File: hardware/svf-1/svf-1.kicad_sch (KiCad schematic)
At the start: 75 parts, among them J1 MonoJack, J2 MonoJack, J3 MonoJack, J4 MonoJack, J5 MonoJack, J6 MonoJack, J7 MonoJack, J8 MonoJack, J9 IDC Header 10P, Q1 MMDT5401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

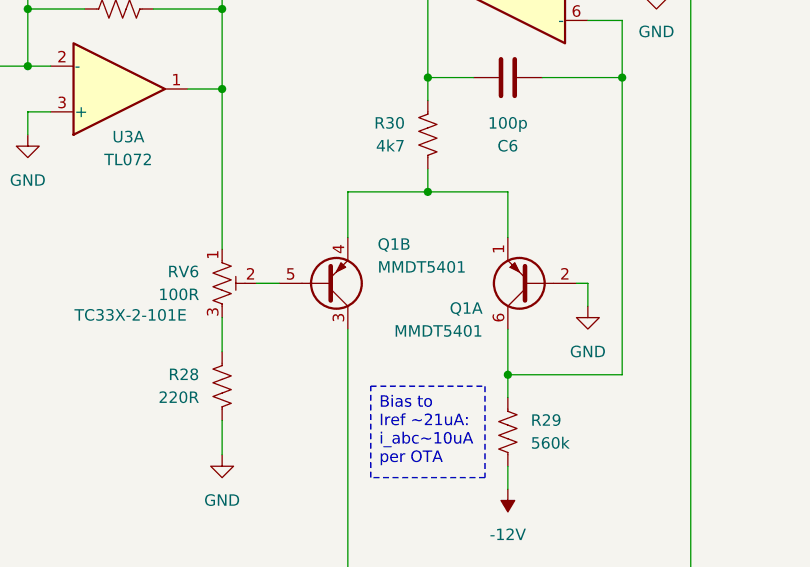
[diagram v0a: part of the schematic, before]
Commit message: Schematic and PBC fix: replace incorrect MMDT5401 (SOT-363) with DMMT5401 (SOT-236) part
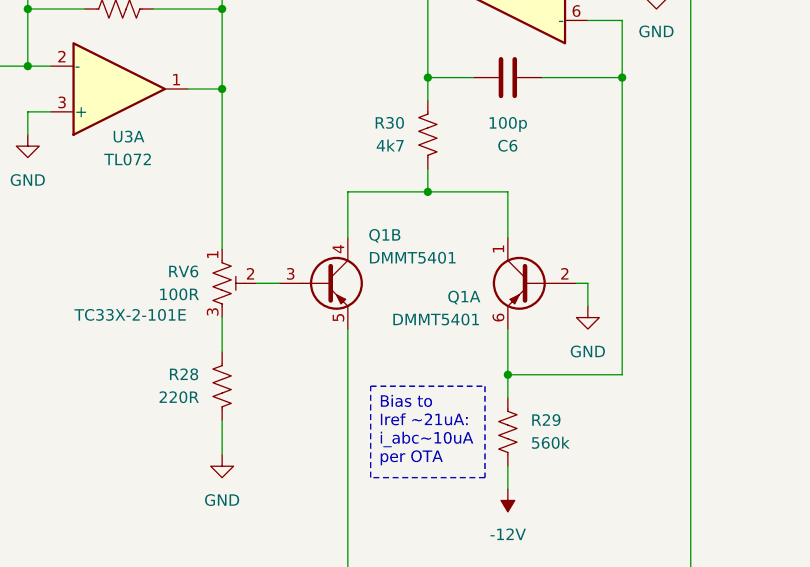
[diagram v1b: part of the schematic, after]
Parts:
- removed Q1: MMDT5401, Package_TO_SOT_SMD:SOT-363_SC-70-6, symbol Transistor_BJT:MMDT5401
- added Q1: DMMT5401, Package_TO_SOT_SMD:SOT-23-6, symbol Transistor_BJT:DMMT5401
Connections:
- net GND: now also Q1.2 (B1)
- net at C6.1, R29.2, U3.6 (-): now also Q1.6 (E1)
- net at R30.1: now also Q1.1 (C1), Q1.4 (C2)
- net at R17.1, R9.1: now also Q1.5 (E2)
- net at RV6.2: now also Q1.3 (B2)
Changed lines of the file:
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@@
 	(title_block
 		(title "State Variable Filter")
-		(date "2025-12-14")
-		(rev "1.0")
+		(date "2025-12-28")
+		(rev "1.1")
 		(company "idyllm")
 		(comment 1 "CC BY-SA 4.0")
@@
 	)
 	(symbol
+		(lib_id "Transistor_BJT:DMMT5401")
+		(at 120.65 168.91 0)
+		(mirror y)
+		(unit 1)
+		(exclude_from_sim no)
+		(in_bom yes)
+		(on_board yes)
+		(dnp no)
+		(property "Reference" "Q1"
+			(at 115.062 170.434 0)
+			(effects
+				(font
+					(size 1.27 1.27)
+				)
+				(justify left)
+			)
+		)
+		(property "Value" "DMMT5401"
+			(at 115.062 172.974 0)
+			(effects
+				(font
+					(size 1.27 1.27)
+				)
+				(justify left)
+			)
+		)
+		(property "Footprint" "Package_TO_SOT_SMD:SOT-23-6"
+			(at 115.57 166.37 0)
+			(effects
+				(font
+					(size 1.27 1.27)
+				)
+				(hide yes)
+			)
+		)
+		(property "Datasheet" "https://www.diodes.com/assets/Datasheets/ds30437.pdf"
+			(at 120.65 168.91 0)
+			(effects
+				(font
+					(size 1.27 1.27)
+				)
+				(hide yes)
+			)
+		)
+		(property "Description" "Dual PNP transistor, 6 pin package"
+			(at 120.65 168.91 0)
+			(effects
+				(font
+					(size 1.27 1.27)
+				)
+				(hide yes)
+			)
+		)
+		(pin "1"
+		)
+		(pin "4"
+		)
+		(pin "3"
+		)
+		(pin "6"
+		)
+		(pin "5"
+		)
+		(pin "2"
+		)
+		(instances
+			(project ""
+				(path "/eb791da7-766f-42cc-8763-47037328a8d4"
+					(reference "Q1")
+					(unit 1)
+				)
+			)
+		)
+	)
+	(symbol
 		(lib_id "Device:C")
 		(at 217.17 156.21 0)
@@
 	)
 	(symbol
+		(lib_id "Transistor_BJT:DMMT5401")
+		(at 97.79 168.91 0)
+		(unit 2)
+		(exclude_from_sim no)
+		(in_bom yes)
+		(on_board yes)
+		(dnp no)
+		(property "Reference" "Q1"
+			(at 102.616 163.576 0)
+			(effects
+				(font
+					(size 1.27 1.27)
+				)
+				(justify left)
+			)
+		)
+		(property "Value" "DMMT5401"
+			(at 102.616 166.116 0)
+			(effects
+				(font
+					(size 1.27 1.27)
+				)
+				(justify left)
+			)
+		)
+		(property "Footprint" "Package_TO_SOT_SMD:SOT-23-6"
+			(at 102.87 166.37 0)
+			(effects
+				(font
+					(size 1.27 1.27)
+				)
+				(hide yes)
+			)
+		)
+		(property "Datasheet" "https://www.diodes.com/assets/Datasheets/ds30437.pdf"
+			(at 97.79 168.91 0)
+			(effects
+				(font
+					(size 1.27 1.27)
+				)
+				(hide yes)
+			)
+		)
+		(property "Description" "Dual PNP transistor, 6 pin package"
+			(at 97.79 168.91 0)
+			(effects
+				(font
+					(size 1.27 1.27)
+				)
+				(hide yes)
+			)
+		)
+		(pin "1"
+		)
+		(pin "4"
+		)
+		(pin "3"
+		)
+		(pin "6"
+		)
+		(pin "5"
+		)
+		(pin "2"
+		)
+		(instances
+			(project ""
+				(path "/eb791da7-766f-42cc-8763-47037328a8d4"
+					(reference "Q1")
+					(unit 2)
+				)
+			)
+		)
+	)
+	(symbol
 		(lib_id "Device:C")
 		(at 118.11 146.05 270)
@@
 	)
 	(symbol
-		(lib_id "Transistor_BJT:MMDT5401")
-		(at 120.65 168.91 180)
-		(unit 1)
-		(exclude_from_sim no)
-		(in_bom yes)
-		(on_board yes)
-		(dnp no)
-		(property "Reference" "Q1"
-			(at 115.316 171.704 0)
-			(effects
-				(font
-					(size 1.27 1.27)
-				)
-				(justify left)
-			)
-		)
-		(property "Value" "MMDT5401"
-			(at 115.316 174.244 0)
-			(effects
-				(font
-					(size 1.27 1.27)
-				)
-				(justify left)
-			)
-		)
-		(property "Footprint" "Package_TO_SOT_SMD:SOT-363_SC-70-6"
-			(at 115.57 171.45 0)
-			(effects
-				(font
-					(size 1.27 1.27)
-				)
-				(hide yes)
-			)
-		)
-		(property "Datasheet" "http://www.diodes.com/_files/datasheets/ds30169.pdf"
-			(at 120.65 168.91 0)
-			(effects
-				(font
-					(size 1.27 1.27)
-				)
-				(hide yes)
-			)
-		)
-		(property "Description" "200mA IC, 160V Vce, Dual PNP/PNP Transistors, SOT-363"
-			(at 120.65 168.91 0)
-			(effects
-				(font
-					(size 1.27 1.27)
-				)
-				(hide yes)
-			)
-		)
-		(pin "1"
-		)
-		(pin "6"
-		)
-		(pin "4"
-		)
-		(pin "5"
-		)
-		(pin "3"
-		)
-		(pin "2"
-		)
-		(instances
-			(project ""
-				(path "/eb791da7-766f-42cc-8763-47037328a8d4"
-					(reference "Q1")
-					(unit 1)
-				)
-			)
-		)
-	)
-	(symbol
 		(lib_id "Amplifier_Operational:TL074")
 		(at 152.4 77.47 0)
@@
 				)
 			)
-		)
-	)
-	(symbol
-		(lib_id "Transistor_BJT:MMDT5401")
-		(at 97.79 168.91 0)
-		(mirror x)
-		(unit 2)
-		(exclude_from_sim no)
-		(in_bom yes)
-		(on_board yes)
-		(dnp no)
-		(property "Reference" "Q1"
-			(at 103.632 164.592 0)
-			(effects
-				(font
-					(size 1.27 1.27)
-				)
-				(justify left)
-			)
-		)
-		(property "Value" "MMDT5401"
-			(at 103.632 167.132 0)
-			(effects
-				(font
-					(size 1.27 1.27)
-				)
-				(justify left)
-			)
-		)
-		(property "Footprint" "Package_TO_SOT_SMD:SOT-363_SC-70-6"
-			(at 102.87 171.45 0)
-			(effects
-				(font
-					(size 1.27 1.27)
-				)
-				(hide yes)
-			)
-		)
-		(property "Datasheet" "http://www.diodes.com/_files/datasheets/ds30169.pdf"
-			(at 97.79 168.91 0)
-			(effects
-				(font
-					(size 1.27 1.27)
-				)
-				(hide yes)
-			)
-		)
-		(property "Description" "200mA IC, 160V Vce, Dual PNP/PNP Transistors, SOT-363"
-			(at 97.79 168.91 0)
-			(effects
-				(font
-					(size 1.27 1.27)
-				)
-				(hide yes)
-			)
-		)
-		(pin "1"
-		)
-		(pin "6"
-		)
-		(pin "4"
-		)
-		(pin "5"
-		)
-		(pin "3"
-		)
-		(pin "2"
-		)
-		(instances
-			(project ""
-				(path "/eb791da7-766f-42cc-8763-47037328a8d4"
-					(reference "Q1")
-					(unit 2)
-				)
-			)

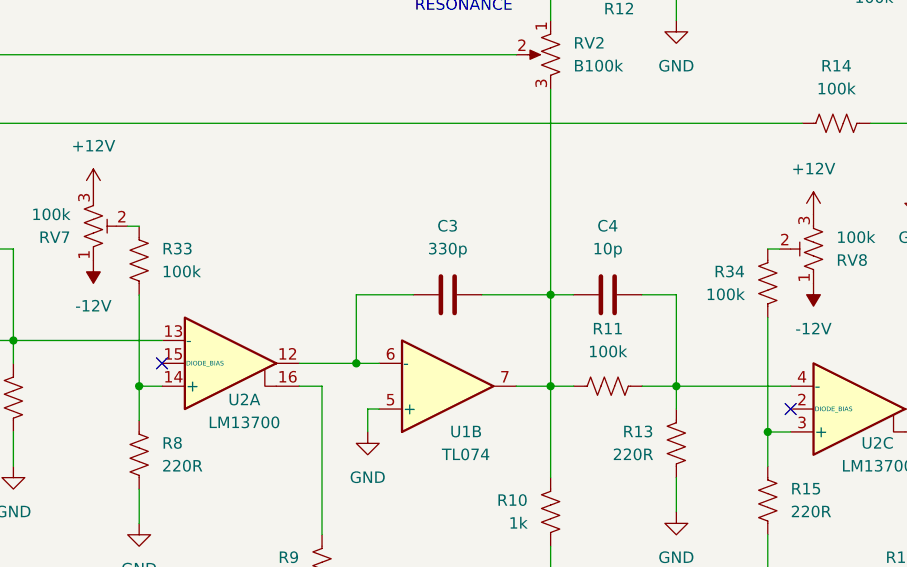
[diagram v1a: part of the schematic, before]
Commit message: Updated docs and design after building and testing the PCB
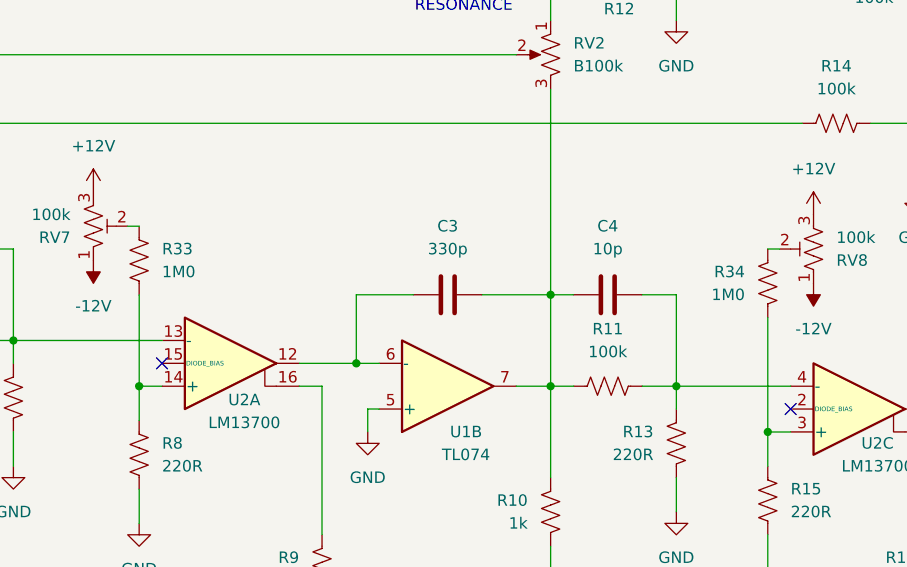
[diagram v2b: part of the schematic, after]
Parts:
- R33, R34: value 100k -> 1M0
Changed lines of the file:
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@@
 	(title_block
 		(title "State Variable Filter")
-		(date "2025-12-28")
+		(date "2026-01-02")
 		(rev "1.1")
 		(company "idyllm")
@@
 			)
 		)
-		(property "Value" "100k"
+		(property "Value" "1M0"
 			(at 185.42 67.3099 0)
 			(effects
@@
 			)
 		)
-		(property "Value" "100k"
+		(property "Value" "1M0"
 			(at 120.65 64.7699 0)
 			(effects

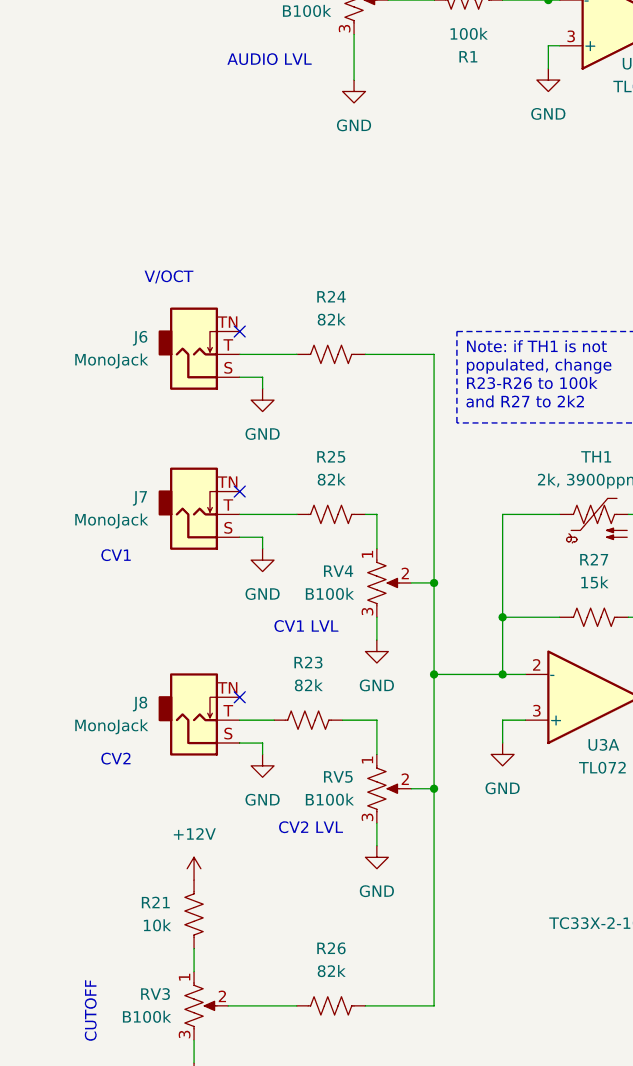
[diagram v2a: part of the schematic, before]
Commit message: Fix CV input pots and Rs
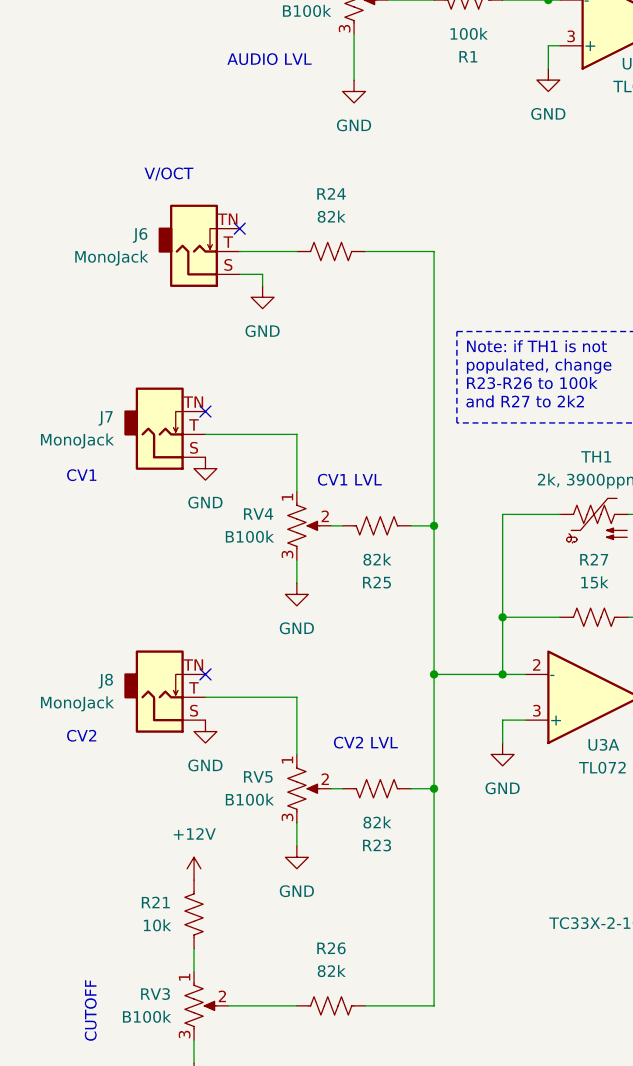
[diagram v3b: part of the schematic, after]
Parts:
- Q1: footprint Package_TO_SOT_SMD:SOT-23-6 -> Package_TO_SOT_SMD:SOT-23-6_Handsoldering
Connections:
- net at RV5.1: now also J8.T; no longer R23.2
- net at R24.2, R26.2, R27.1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: now also R23.2, R25.2; no longer RV4.2, RV5.2
- net at R23.1: now also RV5.2; no longer J8.T
- net at RV4.1: now also J7.T; no longer R25.2
- net at R25.1: now also RV4.2; no longer J7.T
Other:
- moved on the sheet: J6, J7, J8, R23, R24, R25, RV4, RV5

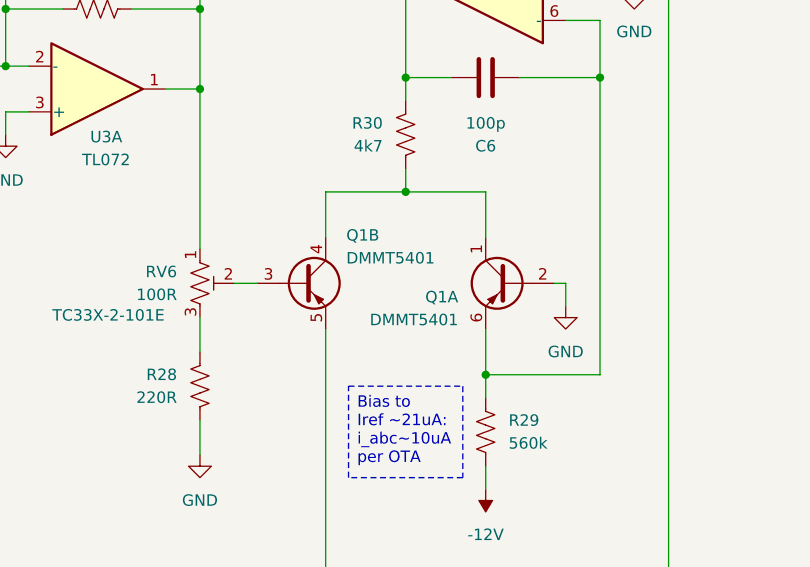
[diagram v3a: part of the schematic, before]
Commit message: Fix for flipped PNP wiring
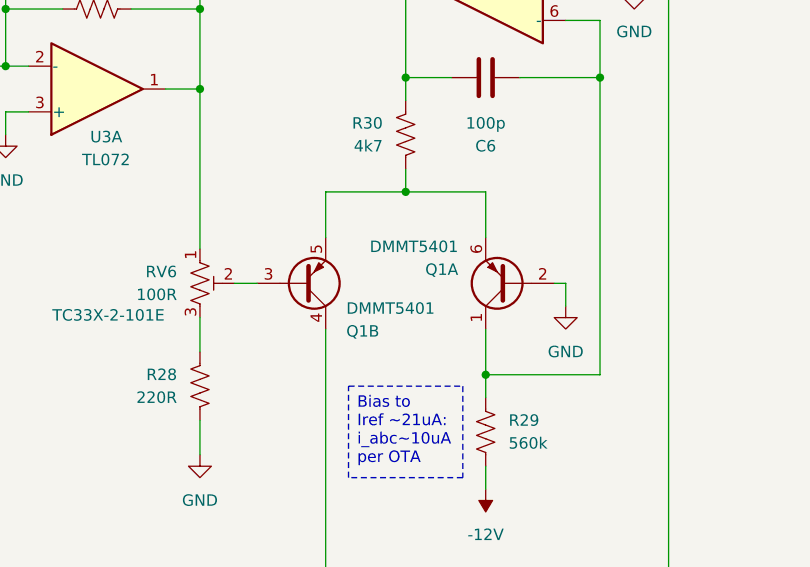
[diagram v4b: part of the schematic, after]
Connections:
- net at C6.1, R29.2, U3.6 (-): now also Q1.1 (C1); no longer Q1.6 (E1)
- net at R17.1, R9.1: now also Q1.4 (C2); no longer Q1.5 (E2)
- new net: Q1.5 (E2), Q1.6 (E1), R30.1
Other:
- moved on the sheet: Q1A
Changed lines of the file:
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@@
 	(title_block
 		(title "State Variable Filter")
-		(date "2026-01-03")
-		(rev "1.1")
+		(date "2026-02-10")
+		(rev "1.2")
 		(company "idyllm")
 		(comment 1 "CC BY-SA 4.0")
@@
 	(symbol
 		(lib_id "Transistor_BJT:DMMT5401")
-		(at 120.65 168.91 0)
-		(mirror y)
+		(at 120.65 168.91 180)
 		(unit 1)
 		(exclude_from_sim no)
@@
 		(dnp no)
 		(property "Reference" "Q1"
-			(at 115.062 170.434 0)
+			(at 115.062 167.386 0)
 			(effects
 				(font
@@
 		)
 		(property "Value" "DMMT5401"
-			(at 115.062 172.974 0)
+			(at 115.062 164.846 0)
 			(effects
 				(font
@@
 		)
 		(property "Footprint" "Package_TO_SOT_SMD:SOT-23-6_Handsoldering"
-			(at 115.57 166.37 0)
+			(at 115.57 171.45 0)
 			(effects
 				(font
@@
 		(lib_id "Transistor_BJT:DMMT5401")
 		(at 97.79 168.91 0)
+		(mirror x)
 		(unit 2)
 		(exclude_from_sim no)
@@
 		(dnp no)
 		(property "Reference" "Q1"
-			(at 102.616 163.576 0)
+			(at 102.616 174.244 0)
 			(effects
 				(font
@@
 		)
 		(property "Value" "DMMT5401"
-			(at 102.616 166.116 0)
+			(at 102.616 171.704 0)
 			(effects
 				(font
@@
 		)
 		(property "Footprint" "Package_TO_SOT_SMD:SOT-23-6_Handsoldering"
-			(at 102.87 166.37 0)
+			(at 102.87 171.45 0)
 			(effects
 				(font
